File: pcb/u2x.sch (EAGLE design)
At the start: 29 parts, among them IC1 LD117AS33TR, IC2 LD117AS25TR, IC3 LD117AS12TR, SW20 324_SW, U1 USB251XB, U3 USBC_16P, U5 CH340C, X1 USB2, X8 USB2

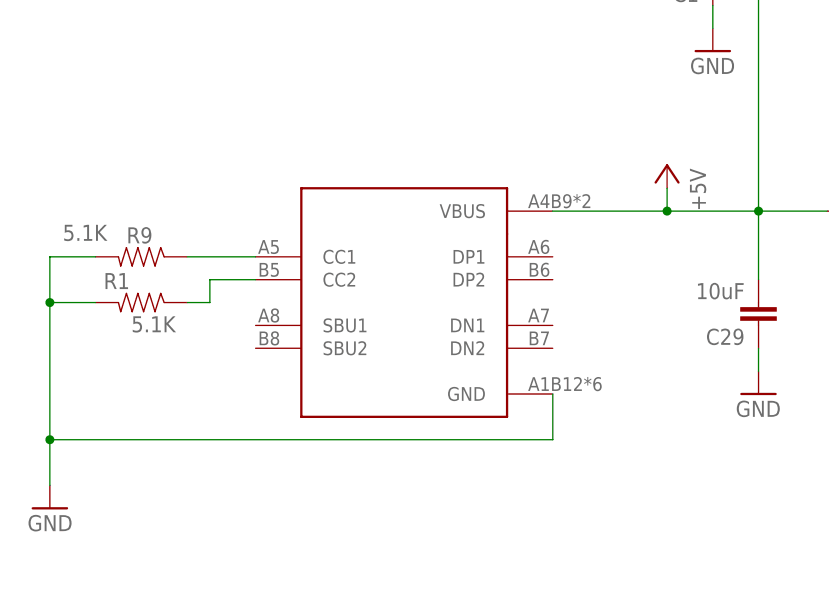
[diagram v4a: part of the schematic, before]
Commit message: switched to sparkfuns usbc
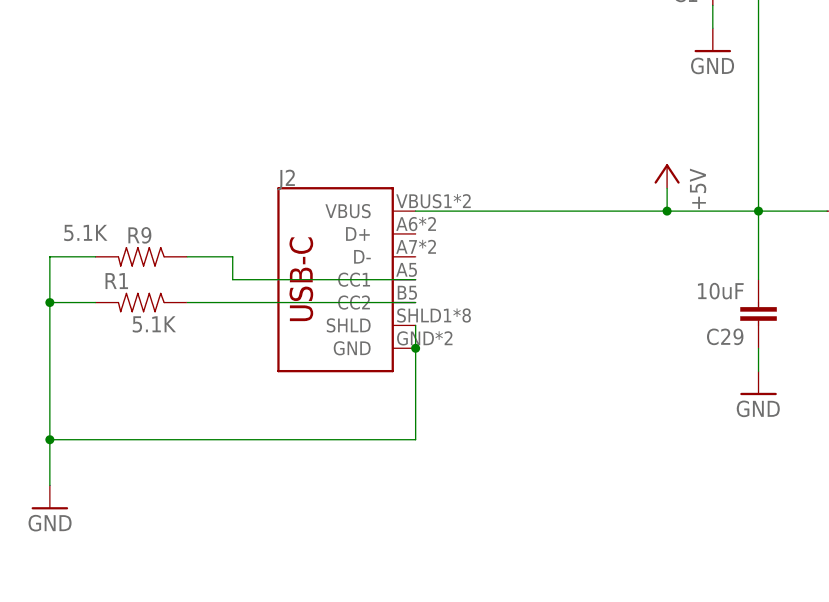
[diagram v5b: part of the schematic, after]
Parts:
- removed U3: USBC_16P, my_usbc_16p:USBC_16P
- added J2: (no value), SparkFun-Connectors:USB_C16PIN
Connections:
- removed net N$1: R9.1, U3.CC1
- new net N$7: J2.CC2, R1.1
- net +5V: now also J2.VBUS; no longer U3.VBUS
- net GND: now also J2.GND, J2.SHLD; no longer U3.GND
- net N$2: now also J2.CC1, R9.1; no longer R1.1, U3.CC2
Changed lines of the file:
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@@
 </classes>
 <parts>
-<part name="U3" library="my_usbc_16p" deviceset="USBC_16P" device=""/>
 <part name="SD1" library="clock" deviceset="TF-HOLDER" device=""/>
 <part name="SW20" library="3pos_slide_switch_centered" deviceset="324_SW" device="" value="324_SW"/>
@@
 <part name="LED3" library="adafruit" deviceset="LED" device="CHIP-LED0805"/>
 <part name="R3" library="SparkFun-Passives" deviceset="RESISTOR" device="0805-RES" value="1K"/>
+<part name="J2" library="SparkFun-Connectors" deviceset="USB_C" device="16PIN"/>
 </parts>
 <sheets>
@@
 </plain>
 <instances>
-<instance part="U3" gate="G$1" x="-154.94" y="-7.62" smashed="yes" rot="MR0"/>
 <instance part="SD1" gate="G$1" x="-76.2" y="81.28" smashed="yes" rot="MR0">
 <attribute name="NAME" x="-71.12" y="94.488" size="1.6764" layer="95" rot="MR0"/>
@@
 <attribute name="NAME" x="-67.31" y="105.1814" size="1.778" layer="95" rot="R180"/>
 <attribute name="VALUE" x="-67.31" y="109.982" size="1.778" layer="96" rot="R180"/>
+</instance>
+<instance part="J2" gate="J1" x="-167.64" y="5.08" smashed="yes">
+<attribute name="VALUE" x="-170.18" y="-7.366" size="1.778" layer="96" font="vector" rot="MR180" align="top-left"/>
+<attribute name="NAME" x="-170.18" y="15.494" size="1.778" layer="95" font="vector"/>
 </instance>
 </instances>
@@
 <wire x1="-190.5" y1="2.54" x2="-195.58" y2="2.54" width="0.1524" layer="91"/>
 <junction x="-195.58" y="2.54"/>
-<pinref part="U3" gate="G$1" pin="GND"/>
-<wire x1="-139.7" y1="-7.62" x2="-139.7" y2="-12.7" width="0.1524" layer="91"/>
-<wire x1="-139.7" y1="-12.7" x2="-195.58" y2="-12.7" width="0.1524" layer="91"/>
 <junction x="-195.58" y="-12.7"/>
+<pinref part="J2" gate="J1" pin="SHLD"/>
+<pinref part="J2" gate="J1" pin="GND"/>
+<wire x1="-154.94" y1="-12.7" x2="-195.58" y2="-12.7" width="0.1524" layer="91"/>
+<wire x1="-154.94" y1="0" x2="-154.94" y2="-2.54" width="0.1524" layer="91"/>
+<wire x1="-154.94" y1="-2.54" x2="-154.94" y2="-12.7" width="0.1524" layer="91"/>
+<junction x="-154.94" y="-2.54"/>
 </segment>
 <segment>
@@
 </segment>
 </net>
-<net name="N$1" class="0">
-<segment>
-<pinref part="U3" gate="G$1" pin="CC1"/>
-<pinref part="R9" gate="G$1" pin="1"/>
-<wire x1="-172.72" y1="7.62" x2="-180.34" y2="7.62" width="0.1524" layer="91"/>
-</segment>
-</net>
-<net name="N$2" class="0">
-<segment>
-<pinref part="U3" gate="G$1" pin="CC2"/>
-<wire x1="-172.72" y1="5.08" x2="-177.8" y2="5.08" width="0.1524" layer="91"/>
-<wire x1="-177.8" y1="5.08" x2="-177.8" y2="2.54" width="0.1524" layer="91"/>
-<pinref part="R1" gate="G$1" pin="1"/>
-<wire x1="-177.8" y1="2.54" x2="-180.34" y2="2.54" width="0.1524" layer="91"/>
-</segment>
-</net>
 <net name="+5V" class="0">
 <segment>
-<pinref part="U3" gate="G$1" pin="VBUS"/>
 <pinref part="P+1" gate="1" pin="+5V"/>
-<wire x1="-139.7" y1="12.7" x2="-127" y2="12.7" width="0.1524" layer="91"/>
 <wire x1="-127" y1="12.7" x2="-127" y2="15.24" width="0.1524" layer="91"/>
 <pinref part="IC1" gate="G$1" pin="IN"/>
 <wire x1="-127" y1="12.7" x2="-116.84" y2="12.7" width="0.1524" layer="91"/>
-<junction x="-127" y="12.7"/>
 <pinref part="IC2" gate="G$1" pin="IN"/>
 <wire x1="-116.84" y1="12.7" x2="-109.22" y2="12.7" width="0.1524" layer="91"/>
@@
 <wire x1="-116.84" y1="43.18" x2="-121.92" y2="43.18" width="0.1524" layer="91"/>
 <junction x="-116.84" y="43.18"/>
+<pinref part="J2" gate="J1" pin="VBUS"/>
+<wire x1="-154.94" y1="12.7" x2="-127" y2="12.7" width="0.1524" layer="91"/>
+<junction x="-127" y="12.7"/>
 </segment>
 </net>
@@
 </segment>
 </net>
+<net name="N$2" class="0">
+<segment>
+<pinref part="J2" gate="J1" pin="CC1"/>
+<wire x1="-154.94" y1="5.08" x2="-175.26" y2="5.08" width="0.1524" layer="91"/>
+<wire x1="-175.26" y1="5.08" x2="-175.26" y2="7.62" width="0.1524" layer="91"/>
+<pinref part="R9" gate="G$1" pin="1"/>
+<wire x1="-175.26" y1="7.62" x2="-180.34" y2="7.62" width="0.1524" layer="91"/>
+</segment>
+</net>
+<net name="N$7" class="0">
+<segment>
+<pinref part="J2" gate="J1" pin="CC2"/>
+<pinref part="R1" gate="G$1" pin="1"/>
+<wire x1="-154.94" y1="2.54" x2="-180.34" y2="2.54" width="0.1524" layer="91"/>
+</segment>
+</net>

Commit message: connecting power, sd card, and crystal
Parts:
- added C4: 1uF, clock:CAP0805
- added C8, C9: 18pF, clock:CAP0805
- added Y1: 24MHz, SparkFun-Clocks:CRYSTAL-26MHZSMD-3.2X2.5
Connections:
- new net +1V2: C3.2, IC3.OUT, U$1.VDD-CORE, U$1.VDD-CORE-1, U$1.VDD-CORE-2
- new net +2V5: C2.2, IC2.OUT, U$1.AVCC, U$1.VCC-DRAM0, U$1.VCC-DRAM1, U$1.VCC-DRAM2, U$1.VCC-DRAM3, U$1.VCC-DRAM4
- new net N$1: SD1.DAT1, U$1.PF0
- new net N$10: SD1.CMD(DI), U$1.PF3
- new net N$11: SD1.CD/DAT3(!CS!), U$1.PF4
- new net N$12: SD1.DAT2, U$1.PF5
- new net N$8: SD1.DAT0(DO), U$1.PF1
- new net N$9: SD1.CLK(SCLK), U$1.PF2
- net +3V3: now also C4.2, JP1.1, JP1.17, SD1.VDD, U$1.TV-VCC, U$1.UVCC, U$1.VCC-IO-0, U$1.VCC-IO-1, U$1.VCC-IO-2
- net +5V: now also JP1.2, JP1.4
- net GND: now also C4.1, C8.2, C9.2, JP1.14, JP1.20, JP1.25, JP1.30, JP1.34, JP1.39, JP1.6, JP1.9, SD1.S1, SD1.S2, SD1.S3, SD1.S4, SD1.VSS, U$1.AGND, U$1.PAD, U$1.TV-GND, Y1.3
- net N$3: now also C8.1, U$1.HOSCI, Y1.1; no longer C2.2, IC2.OUT
- net N$4: now also C9.1, U$1.HOSCO, Y1.2; no longer C3.2, IC3.OUT
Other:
- moved on the sheet: SD1

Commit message: routing traces
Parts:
- added C10, C11, C12, C13, C14, C15, C16, C17, C18, C5, C6, C7: 1uF, clock:CAP0805
- added R2, R5, R6: 10K, SparkFun-Passives:RESISTOR0805-RES
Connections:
- new net N$13: U$1.USB-DM, U1.USBDM_UP
- new net N$14: R5.2, R6.1, U$1.SVREF
- new net N$15: U$1.USB-DP, U1.USBDP_UP
- new net N$16: J2.D+, U5.UD+
- new net N$17: JP1.13, R2.2, SW20.2, SW20.3, U$1.RESET
- new net N$18: J2.D-, U5.UD-
- new net N$19: JP1.26, U$1.PE2
- new net N$20: JP1.28, U$1.PE3
- new net N$21: JP1.27, U$1.PE4
- new net N$22: JP1.18, U$1.TPY1
- new net N$23: JP1.22, U$1.TPY2
- new net N$24: JP1.15, U$1.TPX2
- new net N$25: JP1.16, U$1.TPX1
- new net N$26: JP1.29, U$1.PE5
- new net N$27: JP1.32, U$1.PE6
- new net N$28: JP1.31, U$1.PE7
- new net N$29: JP1.33, U$1.PE8
- new net N$30: JP1.36, U$1.PE9
- new net N$31: JP1.35, U$1.PE10
- new net N$32: JP1.38, U$1.PD18
- new net N$33: JP1.40, U$1.PD15
- new net N$34: JP1.37, U$1.PD16
- new net SPI0_CLK: JP1.23, U$1.PC0
- new net SPI0_CS: JP1.24, U$1.PC1
- new net SPI0_MISO: JP1.21, U$1.PC2
- new net SPI0_MOSI: JP1.19, U$1.PC3
- new net TWI0_SCL: JP1.5, U$1.PE11
- new net TWI0_SDA: JP1.3, U$1.PE12
- new net UART0_RX: U$1.PE0, U5.TXO
- new net UART0_TX: U$1.PE1, U5.RXI
- new net UART2_RX: JP1.10, U$1.PD14
- new net UART2_TX: JP1.8, U$1.PD13
- net +1V2: now also C13.2, C16.2, C7.2
- net +2V5: now also C10.2, C11.2, C12.2, C6.2, R5.1
- net +3V3: now also C14.2, C15.2, C17.2, C18.2, C5.2, R2.1
- net GND: now also C10.1, C11.1, C12.1, C13.1, C14.1, C15.1, C16.1, C17.1, C18.1, C5.1, C6.1, C7.1, R6.2, SW20.1, SW20.4
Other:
- moved on the sheet: C1, C2, C27, C29, C3, C4, C8, C9, IC1, IC2, IC3, J2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

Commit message: hooked up ch340, fine tuned traces
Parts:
- added C19: 1uF, clock:CAP0805
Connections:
- net +3V3: now also C19.2, LED1.A, LED3.A, U5.V3, U5.VCC
- net GND: now also C19.1, U5.GND
- net UART0_RX: now also R3.1
- net UART0_TX: now also R4.1
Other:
- moved on the sheet: LED1, LED3, R3, R4, U5
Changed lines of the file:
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@@
 <part name="C17" library="clock" deviceset="CAP" device="0805" value="1uF"/>
 <part name="C18" library="clock" deviceset="CAP" device="0805" value="1uF"/>
+<part name="+3V11" library="supply1" library_urn="urn:adsk.eagle:library:371" deviceset="+3V3" device=""/>
+<part name="GND25" library="supply1" library_urn="urn:adsk.eagle:library:371" deviceset="GND" device=""/>
+<part name="C19" library="clock" deviceset="CAP" device="0805" value="1uF"/>
+<part name="+3V12" library="supply1" library_urn="urn:adsk.eagle:library:371" deviceset="+3V3" device=""/>
+<part name="+3V13" library="supply1" library_urn="urn:adsk.eagle:library:371" deviceset="+3V3" device=""/>
 </parts>
 <sheets>
@@
 <attribute name="VALUE" x="655.32" y="73.66" size="1.778" layer="96"/>
 </instance>
-<instance part="U5" gate="U1" x="447.04" y="60.96" smashed="yes" rot="MR0">
-<attribute name="NAME" x="454.66" y="71.755" size="1.778" layer="95" font="vector" rot="MR0"/>
-<attribute name="VALUE" x="454.66" y="45.72" size="1.778" layer="96" font="vector" rot="MR0"/>
-</instance>
-<instance part="LED1" gate="G$1" x="-81.28" y="116.84" smashed="yes" rot="R90">
-<attribute name="NAME" x="-76.708" y="120.396" size="1.778" layer="95" rot="R180"/>
-<attribute name="VALUE" x="-76.708" y="122.555" size="1.778" layer="96" rot="R180"/>
-</instance>
-<instance part="R4" gate="G$1" x="-71.12" y="116.84" smashed="yes" rot="R180">
-<attribute name="NAME" x="-67.31" y="115.3414" size="1.778" layer="95" rot="R180"/>
-<attribute name="VALUE" x="-67.31" y="120.142" size="1.778" layer="96" rot="R180"/>
-</instance>
-<instance part="LED3" gate="G$1" x="-81.28" y="106.68" smashed="yes" rot="R90">
-<attribute name="NAME" x="-76.708" y="110.236" size="1.778" layer="95" rot="R180"/>
-<attribute name="VALUE" x="-76.708" y="112.395" size="1.778" layer="96" rot="R180"/>
-</instance>
-<instance part="R3" gate="G$1" x="-71.12" y="106.68" smashed="yes" rot="R180">
-<attribute name="NAME" x="-67.31" y="105.1814" size="1.778" layer="95" rot="R180"/>
-<attribute name="VALUE" x="-67.31" y="109.982" size="1.778" layer="96" rot="R180"/>
+<instance part="U5" gate="U1" x="459.74" y="60.96" smashed="yes" rot="MR0">
+<attribute name="NAME" x="467.36" y="71.755" size="1.778" layer="95" font="vector" rot="MR0"/>
+<attribute name="VALUE" x="467.36" y="45.72" size="1.778" layer="96" font="vector" rot="MR0"/>
+</instance>
+<instance part="LED1" gate="G$1" x="444.5" y="91.44" smashed="yes">
+<attribute name="NAME" x="448.056" y="86.868" size="1.778" layer="95" rot="R90"/>
+<attribute name="VALUE" x="450.215" y="86.868" size="1.778" layer="96" rot="R90"/>
+</instance>
+<instance part="R4" gate="G$1" x="444.5" y="78.74" smashed="yes" rot="R90">
+<attribute name="NAME" x="443.0014" y="74.93" size="1.778" layer="95" rot="R90"/>
+<attribute name="VALUE" x="447.802" y="74.93" size="1.778" layer="96" rot="R90"/>
+</instance>
+<instance part="LED3" gate="G$1" x="434.34" y="91.44" smashed="yes">
+<attribute name="NAME" x="437.896" y="86.868" size="1.778" layer="95" rot="R90"/>
+<attribute name="VALUE" x="440.055" y="86.868" size="1.778" layer="96" rot="R90"/>
+</instance>
+<instance part="R3" gate="G$1" x="434.34" y="78.74" smashed="yes" rot="R90">
+<attribute name="NAME" x="432.8414" y="74.93" size="1.778" layer="95" rot="R90"/>
+<attribute name="VALUE" x="437.642" y="74.93" size="1.778" layer="96" rot="R90"/>
 </instance>
 <instance part="J2" gate="J1" x="525.78" y="86.36" smashed="yes">
@@
 <attribute name="NAME" x="618.236" y="42.799" size="1.778" layer="95" rot="R180"/>
 <attribute name="VALUE" x="618.236" y="47.879" size="1.778" layer="96" rot="R180"/>
+</instance>
+<instance part="+3V11" gate="G$1" x="474.98" y="76.2" smashed="yes" rot="MR0">
+<attribute name="VALUE" x="477.52" y="71.12" size="1.778" layer="96" rot="MR90"/>
+</instance>
+<instance part="GND25" gate="1" x="474.98" y="48.26" smashed="yes">
+<attribute name="VALUE" x="472.44" y="45.72" size="1.778" layer="96"/>
+</instance>
+<instance part="C19" gate="G$1" x="581.66" y="45.72" smashed="yes" rot="R180">
+<attribute name="NAME" x="580.136" y="42.799" size="1.778" layer="95" rot="R180"/>
+<attribute name="VALUE" x="580.136" y="47.879" size="1.778" layer="96" rot="R180"/>
+</instance>
+<instance part="+3V12" gate="G$1" x="434.34" y="101.6" smashed="yes" rot="MR0">
+<attribute name="VALUE" x="436.88" y="96.52" size="1.778" layer="96" rot="MR90"/>
+</instance>
+<instance part="+3V13" gate="G$1" x="444.5" y="101.6" smashed="yes" rot="MR0">
+<attribute name="VALUE" x="447.04" y="96.52" size="1.778" layer="96" rot="MR90"/>
 </instance>
 </instances>
@@
 <segment>
 <pinref part="GND22" gate="1" pin="GND"/>
-<wire x1="589.28" y1="40.64" x2="553.72" y2="40.64" width="0.1524" layer="91"/>
+<wire x1="589.28" y1="40.64" x2="581.66" y2="40.64" width="0.1524" layer="91"/>
+<wire x1="581.66" y1="40.64" x2="553.72" y2="40.64" width="0.1524" layer="91"/>
 <wire x1="589.28" y1="40.64" x2="596.9" y2="40.64" width="0.1524" layer="91"/>
 <junction x="589.28" y="40.64"/>
@@
 <junction x="612.14" y="40.64"/>
 <pinref part="C18" gate="G$1" pin="1"/>
+<pinref part="C19" gate="G$1" pin="1"/>
+<junction x="581.66" y="40.64"/>
 </segment>
 <segment>
@@
 <junction x="607.06" y="-22.86"/>
 </segment>
+<segment>
+<pinref part="U5" gate="U1" pin="GND"/>
+<pinref part="GND25" gate="1" pin="GND"/>
+<wire x1="469.9" y1="50.8" x2="474.98" y2="50.8" width="0.1524" layer="91"/>
+</segment>
 </net>
 <net name="+5V" class="0">
@@
 <pinref part="+3V10" gate="G$1" pin="+3V3"/>
 <wire x1="589.28" y1="53.34" x2="589.28" y2="48.26" width="0.1524" layer="91"/>
-<wire x1="589.28" y1="48.26" x2="553.72" y2="48.26" width="0.1524" layer="91"/>
+<wire x1="589.28" y1="48.26" x2="581.66" y2="48.26" width="0.1524" layer="91"/>
+<wire x1="581.66" y1="48.26" x2="553.72" y2="48.26" width="0.1524" layer="91"/>
 <wire x1="589.28" y1="48.26" x2="596.9" y2="48.26" width="0.1524" layer="91"/>
 <junction x="589.28" y="48.26"/>
@@
 <junction x="612.14" y="48.26"/>
 <pinref part="C18" gate="G$1" pin="2"/>
+<pinref part="C19" gate="G$1" pin="2"/>
+<junction x="581.66" y="48.26"/>
+</segment>
+<segment>
+<pinref part="U5" gate="U1" pin="VCC"/>
+<pinref part="+3V11" gate="G$1" pin="+3V3"/>
+<wire x1="469.9" y1="68.58" x2="474.98" y2="68.58" width="0.1524" layer="91"/>
+<wire x1="474.98" y1="68.58" x2="474.98" y2="73.66" width="0.1524" layer="91"/>
+<pinref part="U5" gate="U1" pin="V3"/>
+<wire x1="469.9" y1="66.04" x2="474.98" y2="66.04" width="0.1524" layer="91"/>
+<wire x1="474.98" y1="66.04" x2="474.98" y2="68.58" width="0.1524" layer="91"/>
+<junction x="474.98" y="68.58"/>
+</segment>
+<segment>
+<pinref part="LED3" gate="G$1" pin="A"/>
+<pinref part="+3V12" gate="G$1" pin="+3V3"/>
+<wire x1="434.34" y1="99.06" x2="434.34" y2="93.98" width="0.1524" layer="91"/>
+</segment>
+<segment>
+<pinref part="LED1" gate="G$1" pin="A"/>
+<pinref part="+3V13" gate="G$1" pin="+3V3"/>
+<wire x1="444.5" y1="99.06" x2="444.5" y2="93.98" width="0.1524" layer="91"/>
 </segment>
 </net>
@@
 <pinref part="LED1" gate="G$1" pin="C"/>
 <pinref part="R4" gate="G$1" pin="2"/>
+<wire x1="444.5" y1="86.36" x2="444.5" y2="83.82" width="0.1524" layer="91"/>
 </segment>
 </net>
@@
 <pinref part="LED3" gate="G$1" pin="C"/>
 <pinref part="R3" gate="G$1" pin="2"/>
+<wire x1="434.34" y1="86.36" x2="434.34" y2="83.82" width="0.1524" layer="91"/>
 </segment>
 </net>
@@
 <pinref part="U$1" gate="G$1" pin="PE0"/>
 <pinref part="U5" gate="U1" pin="TXO"/>
-<wire x1="287.02" y1="68.58" x2="436.88" y2="68.58" width="0.1524" layer="91"/>
+<wire x1="287.02" y1="68.58" x2="434.34" y2="68.58" width="0.1524" layer="91"/>
 <label x="292.1" y="68.58" size="1.778" layer="95"/>
-<label x="421.64" y="68.58" size="1.778" layer="95"/>
+<label x="431.8" y="68.58" size="1.778" layer="95"/>
+<pinref part="R3" gate="G$1" pin="1"/>
+<wire x1="434.34" y1="68.58" x2="449.58" y2="68.58" width="0.1524" layer="91"/>
+<wire x1="434.34" y1="73.66" x2="434.34" y2="68.58" width="0.1524" layer="91"/>
+<junction x="434.34" y="68.58"/>
 </segment>
 </net>
@@
 <pinref part="U$1" gate="G$1" pin="PE1"/>
 <pinref part="U5" gate="U1" pin="RXI"/>
-<wire x1="287.02" y1="66.04" x2="436.88" y2="66.04" width="0.1524" layer="91"/>
+<wire x1="287.02" y1="66.04" x2="444.5" y2="66.04" width="0.1524" layer="91"/>
 <label x="292.1" y="66.04" size="1.778" layer="95"/>
-<label x="421.64" y="66.04" size="1.778" layer="95"/>
+<label x="431.8" y="66.04" size="1.778" layer="95"/>
+<pinref part="R4" gate="G$1" pin="1"/>
+<wire x1="444.5" y1="66.04" x2="449.58" y2="66.04" width="0.1524" layer="91"/>
+<wire x1="444.5" y1="73.66" x2="444.5" y2="66.04" width="0.1524" layer="91"/>
+<junction x="444.5" y="66.04"/>
 </segment>
 </net>
@@
 <segment>
 <pinref part="U5" gate="U1" pin="UD+"/>
-<wire x1="457.2" y1="60.96" x2="553.72" y2="60.96" width="0.1524" layer="91"/>
+<wire x1="469.9" y1="60.96" x2="553.72" y2="60.96" width="0.1524" layer="91"/>
 <wire x1="553.72" y1="60.96" x2="553.72" y2="91.44" width="0.1524" layer="91"/>
 <pinref part="J2" gate="J1" pin="D+"/>
@@
 <segment>
 <pinref part="U5" gate="U1" pin="UD-"/>
-<wire x1="457.2" y1="58.42" x2="551.18" y2="58.42" width="0.1524" layer="91"/>
+<wire x1="469.9" y1="58.42" x2="551.18" y2="58.42" width="0.1524" layer="91"/>
 <wire x1="551.18" y1="58.42" x2="551.18" y2="88.9" width="0.1524" layer="91"/>
 <pinref part="J2" gate="J1" pin="D-"/>
